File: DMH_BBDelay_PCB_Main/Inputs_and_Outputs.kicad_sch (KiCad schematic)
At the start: 1 part, among them J200 IDC_02x05

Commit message: Schematic in progress
Next is implementation of Channel B, CV Linking and Ping-Pong mode
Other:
- title: (none) -> 3205 Delay
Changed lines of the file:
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@@
 	(paper "A4" portrait)
 	(title_block
+		(title "3205 Delay")
 		(company "DMH Instruments")
 		(comment 1 "PCB for 10cm Kosmo format synthesizer module")

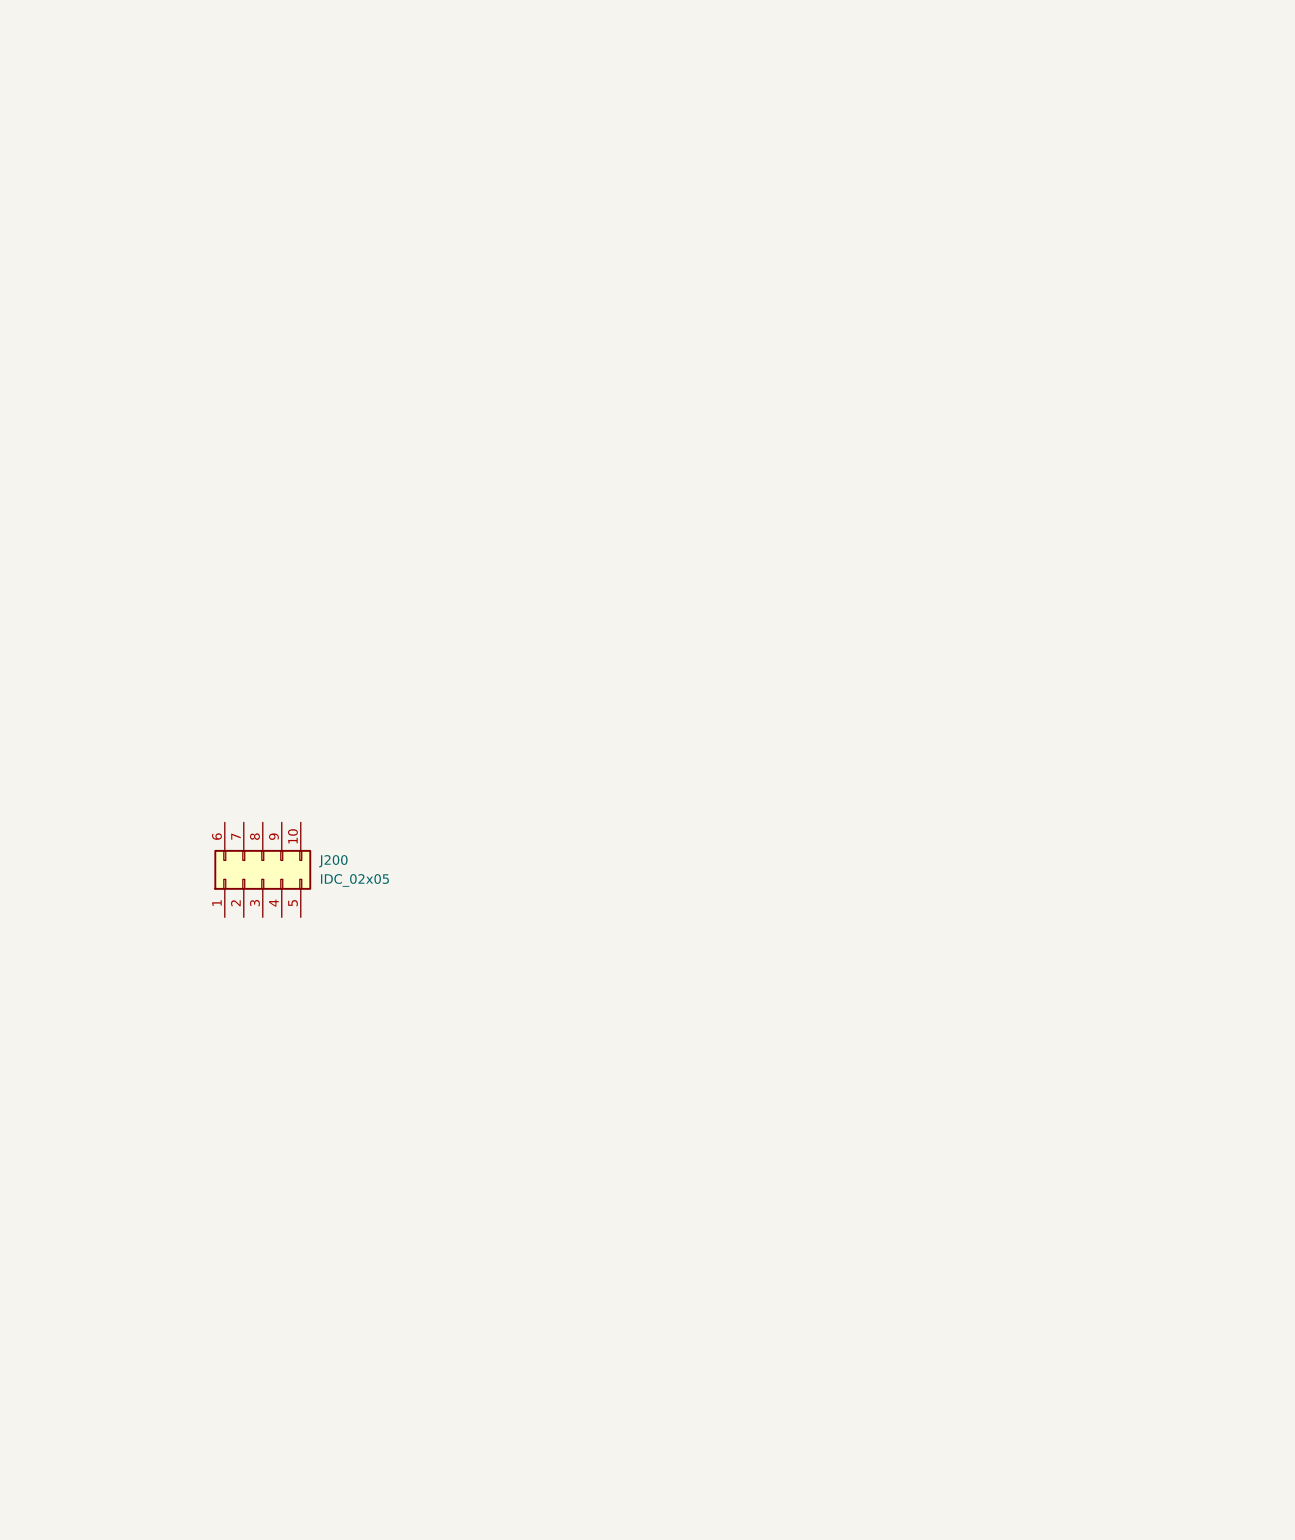
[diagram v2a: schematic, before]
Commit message: Added schmit triggers to inhibt CV input paths
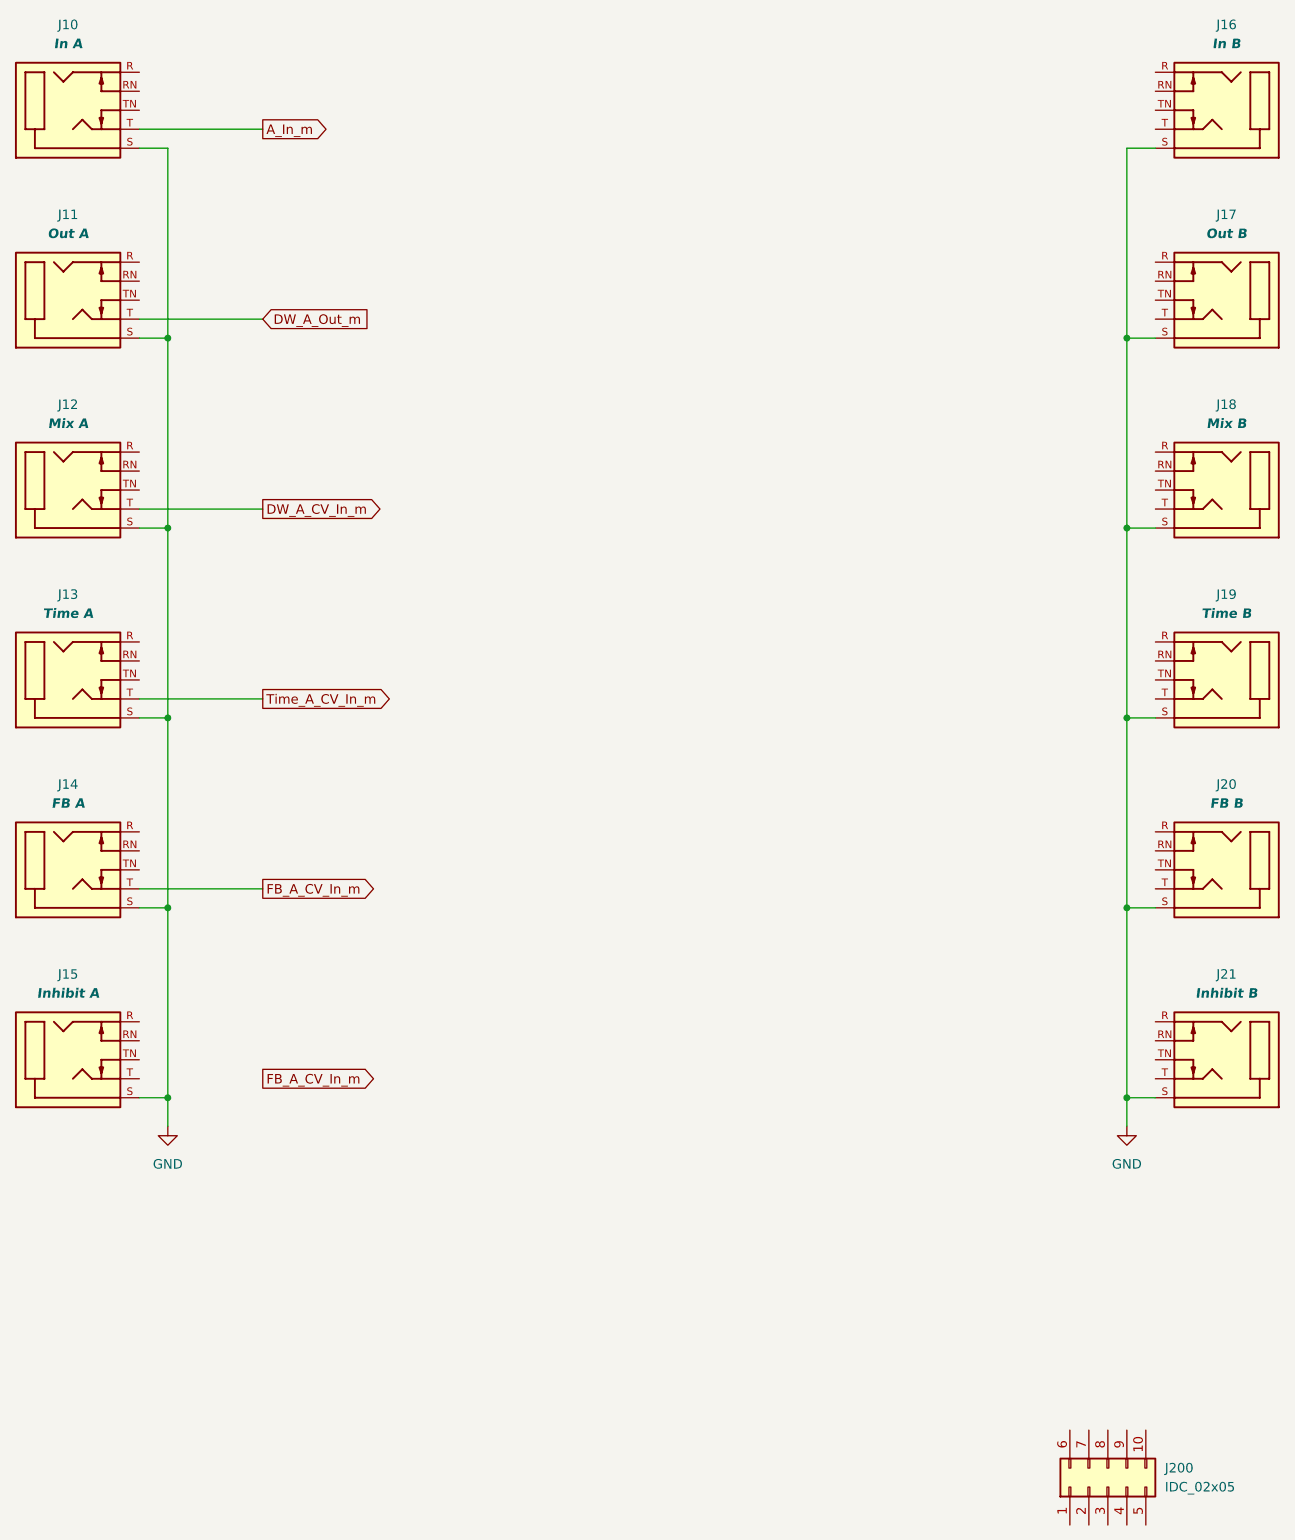
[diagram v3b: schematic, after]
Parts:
- added J10, J11, J12, J13, J14, J15, J16, J17, J18, J19, J20, J21: TRS_Jack_6.35mm_Sw, SynthStuff:CUI_SJ-63083D, symbol SynthStuff:TRS_Jack_6.35mm_Sw
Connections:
- new net A_In_m: J10.T (3)
- new net DW_A_CV_In_m: J12.T (3)
- new net DW_A_Out_m: J11.T (3)
- new net FB_A_CV_In_m: J14.T (3)
- new net GND: J10.S (1), J11.S (1), J12.S (1), J13.S (1), J14.S (1), J15.S (1), J16.S (1), J17.S (1), J18.S (1), J19.S (1), J20.S (1), J21.S (1)
- new net Time_A_CV_In_m: J13.T (3)
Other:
- moved on the sheet: J200

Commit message: Added TRS jacks to IO page
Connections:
- net B_In_m: now reaches J16.T (3)
- net Time_B_CV_In_m: now reaches J19.T (3)
- net FB_B_CV_In_m: now reaches J20.T (3)
- net Inhibt_B_CV_m: now reaches J21.T (3)
- net DW_B_CV_In_m: now reaches J18.T (3)
- net Inhibt_A_CV_m: now reaches J15.T (3)
- net DW_B_Out_m: now reaches J17.T (3)
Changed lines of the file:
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@@
+	(wire
+		(pts
+			(xy 152.4 116.84) (xy 170.18 116.84)
+		)
+		(stroke
+			(width 0)
+			(type default)
+		)
+	)
 	(wire
 		(pts
@@
 	(wire
 		(pts
+			(xy 152.4 142.24) (xy 170.18 142.24)
+		)
+		(stroke
+			(width 0)
+			(type default)
+		)
+	)
+	(wire
+		(pts
+			(xy 34.29 167.64) (xy 50.8 167.64)
+		)
+		(stroke
+			(width 0)
+			(type default)
+		)
+	)
+	(wire
+		(pts
 			(xy 38.1 68.58) (xy 38.1 43.18)
 		)
@@
 	(wire
 		(pts
+			(xy 152.4 40.64) (xy 170.18 40.64)
+		)
+		(stroke
+			(width 0)
+			(type default)
+		)
+	)
+	(wire
+		(pts
 			(xy 166.37 170.18) (xy 166.37 144.78)
 		)
@@
 	(wire
 		(pts
+			(xy 152.4 91.44) (xy 170.18 91.44)
+		)
+		(stroke
+			(width 0)
+			(type default)
+		)
+	)
+	(wire
+		(pts
+			(xy 152.4 167.64) (xy 170.18 167.64)
+		)
+		(stroke
+			(width 0)
+			(type default)
+		)
+	)
+	(wire
+		(pts
 			(xy 166.37 144.78) (xy 166.37 119.38)
 		)
@@
 	(wire
 		(pts
+			(xy 152.4 66.04) (xy 170.18 66.04)
+		)
+		(stroke
+			(width 0)
+			(type default)
+		)
+	)
+	(wire
+		(pts
 			(xy 38.1 173.99) (xy 38.1 170.18)
 		)
@@
 		)
 	)
+	(global_label "Inhibt_A_CV_m"
+		(shape output)
+		(at 50.8 167.64 0)
+		(fields_autoplaced yes)
+		(effects
+			(font
+				(size 1.27 1.27)
+			)
+			(justify left)
+		)
+		(property "Intersheetrefs" "${INTERSHEET_REFS}"
+			(at 67.2108 167.64 0)
+			(hide yes)
+			(show_name no)
+			(do_not_autoplace no)
+			(effects
+				(font
+					(size 1.27 1.27)
+				)
+				(justify left)
+			)
+		)
+	)
+	(global_label "DW_B_CV_In_m"
+		(shape output)
+		(at 152.4 91.44 180)
+		(fields_autoplaced yes)
+		(effects
+			(font
+				(size 1.27 1.27)
+			)
+			(justify right)
+		)
+		(property "Intersheetrefs" "${INTERSHEET_REFS}"
+			(at 135.9287 91.44 0)
+			(hide yes)
+			(show_name no)
+			(do_not_autoplace no)
+			(effects
+				(font
+					(size 1.27 1.27)
+				)
+				(justify right)
+			)
+		)
+	)
+	(global_label "DW_B_Out_m"
+		(shape input)
+		(at 152.4 66.04 180)
+		(fields_autoplaced yes)
+		(effects
+			(font
+				(size 1.27 1.27)
+			)
+			(justify right)
+		)
+		(property "Intersheetrefs" "${INTERSHEET_REFS}"
+			(at 137.8035 66.04 0)
+			(hide yes)
+			(show_name no)
+			(do_not_autoplace no)
+			(effects
+				(font
+					(size 1.27 1.27)
+				)
+				(justify right)
+			)
+		)
+	)
 	(global_label "FB_A_CV_In_m"
 		(shape output)
-		(at 50.8 167.64 0)
+		(at 50.8 142.24 0)
 		(fields_autoplaced yes)
 		(effects
@@
 		)
 		(property "Intersheetrefs" "${INTERSHEET_REFS}"
-			(at 66.9085 167.64 0)
+			(at 66.9085 142.24 0)
 			(hide yes)
 			(show_name no)
@@
 		)
 	)
-	(global_label "FB_A_CV_In_m"
-		(shape output)
-		(at 50.8 142.24 0)
-		(fields_autoplaced yes)
-		(effects
-			(font
-				(size 1.27 1.27)
-			)
-			(justify left)
-		)
-		(property "Intersheetrefs" "${INTERSHEET_REFS}"
-			(at 66.9085 142.24 0)
-			(hide yes)
-			(show_name no)
-			(do_not_autoplace no)
-			(effects
-				(font
-					(size 1.27 1.27)
-				)
-				(justify left)
+	(global_label "B_In_m"
+		(shape output)
+		(at 152.4 40.64 180)
+		(fields_autoplaced yes)
+		(effects
+			(font
+				(size 1.27 1.27)
+			)
+			(justify right)
+		)
+		(property "Intersheetrefs" "${INTERSHEET_REFS}"
+			(at 142.9439 40.64 0)
+			(hide yes)
+			(show_name no)
+			(do_not_autoplace no)
+			(effects
+				(font
+					(size 1.27 1.27)
+				)
+				(justify right)
+			)
+		)
+	)
+	(global_label "Time_B_CV_In_m"
+		(shape output)
+		(at 152.4 116.84 180)
+		(fields_autoplaced yes)
+		(effects
+			(font
+				(size 1.27 1.27)
+			)
+			(justify right)
+		)
+		(property "Intersheetrefs" "${INTERSHEET_REFS}"
+			(at 134.2958 116.84 0)
+			(hide yes)
+			(show_name no)
+			(do_not_autoplace no)
+			(effects
+				(font
+					(size 1.27 1.27)
+				)
+				(justify right)
 			)
 		)
@@
 			)
 		)
+	)
+	(global_label "Inhibt_B_CV_m"
+		(shape output)
+		(at 152.4 167.64 180)
+		(fields_autoplaced yes)
+		(effects
+			(font
+				(size 1.27 1.27)
+			)
+			(justify right)
+		)
+		(property "Intersheetrefs" "${INTERSHEET_REFS}"
+			(at 135.9892 167.64 0)
+			(hide yes)
+			(show_name no)
+			(do_not_autoplace no)
+			(effects
+				(font
+					(size 1.27 1.27)
+				)
+				(justify right)
+			)
+		)
+	)
+	(global_label "FB_B_CV_In_m"
+		(shape output)
+		(at 152.4 142.24 180)
+		(fields_autoplaced yes)
+		(effects
+			(font
+				(size 1.27 1.27)
+			)
+			(justify right)
+		)
+		(property "Intersheetrefs" "${INTERSHEET_REFS}"
+			(at 136.2915 142.24 0)
+			(hide yes)
+			(show_name no)
+			(do_not_autoplace no)
+			(effects
+				(font
+					(size 1.27 1.27)
+				)
+				(justify right)
+			)
+		)
